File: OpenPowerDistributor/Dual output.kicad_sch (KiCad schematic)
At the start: 18 parts, among them J2 Barrel_Jack, Q1 STN2610D, Q2 BC847, Q3 BC847, U3 LM324

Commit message: More schematic progress
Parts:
- removed D7: SMBJ24A, Diode_SMD:D_SMA, symbol Diode:SMAJ12A
- added C10, C11: 100nF 16V, Capacitor_SMD:C_0603_1608Metric, symbol Device:C_Small
- added C12: NA, Capacitor_SMD:C_0603_1608Metric, symbol Device:C_Small
- added D4: SS36(F), Diode_SMD:D_SMA, symbol Device:D_Schottky
- added D6: AZ23C16, Package_TO_SOT_SMD:SOT-23, symbol Device:D_Zener_Dual_CommonAnode_KKA
- added J3: Barrel_Jack, Connector_BarrelJack:BarrelJack_Horizontal, symbol Connector:Barrel_Jack
- added Q4, Q5: BC847, Package_TO_SOT_SMD:SOT-23, symbol Transistor_BJT:BC847
- added Q6: STN2610D, Package_TO_SOT_SMD:TO-252-2, symbol Transistor_FET:IPD50R3K0CE
- added R13, R14, R15, R19: 390k, Resistor_SMD:R_0603_1608Metric, symbol Device:R_Small
- added R16, R17: 1M, Resistor_SMD:R_0603_1608Metric, symbol Device:R_Small
- added R18, R22: 100k, Resistor_SMD:R_0603_1608Metric, symbol Device:R_Small
- added R20: 15k, Resistor_SMD:R_0603_1608Metric, symbol Device:R_Small
- added R21: 33mR, Resistor_SMD:R_1206_3216Metric, symbol Device:R_Small
- C8: footprint (none) -> Capacitor_SMD:C_0603_1608Metric
- D8: footprint (none) -> Package_TO_SOT_SMD:SOT-23
- J2: footprint (none) -> Connector_BarrelJack:BarrelJack_Horizontal
- R10, R9: value 390k -> 1M; footprint (none) -> Resistor_SMD:R_0603_1608Metric
- R11: value 33k -> 100k; footprint (none) -> Resistor_SMD:R_0603_1608Metric
- R12: value 390k -> 100k; footprint (none) -> Resistor_SMD:R_0603_1608Metric
- R6, R7: footprint (none) -> Resistor_SMD:R_0603_1608Metric
- R8: value 15k -> 100k; footprint (none) -> Resistor_SMD:R_0603_1608Metric
- U3: footprint (none) -> Package_SO:TSSOP-14_4.4x5mm_P0.65mm
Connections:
- net +30V: now also R17.1
- net GND: now also Q4.2 (E), Q5.2 (E), R20.1, R21.2
- net V_{In}: now also D4.2 (A)
- net O1+: now reaches D8.2 (K), J2.1, Q1.3 (S), R11.1
- net O1+: no longer J2.2, R11.2, R5.1, U3.5 (+)
- net at R10.1, R12.2, U3.1: now also C10.2
- net at U3.10 (+): now also C11.1, R14.2
- net at U3.8: now also C11.2, R15.2, R16.1
- net Isns2: now reaches U3.9 (-)
- net Isns2: now also U3.14, C12.2, R19.1
- net O2+: now reaches U3.12 (+)
- net O2+: now also D6.2 (K), J3.1, J3.2, Q6.3 (S), R21.1, R22.1, R22.2
- net at U3.13 (-): now also C12.1, R19.2, R20.2
- net Iset: no longer names the net of U3.2 (-)
- net Iset: now also C10.1, R13.2
- net Isns renamed Isns1
- net ~{Overcurrent} renamed ~{Overcurrent}1
- new net: D6.1 (K), Q6.1 (G), R17.2, R18.1
- new net: Q5.3 (C), R18.2
- new net: D4.1 (K), Q6.2 (D)
- new net: Q5.1 (B), R16.2
- new net: Q4.1 (B), R15.1
- new net Iset1: R13.1
- new net Iset2: R14.1
- new net O1-: J2.2, R11.2, R5.1, U3.5 (+)
- new net ~{Overcurrent}2: Q4.3 (C)
- no-connect marks 1 -> 2
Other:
- note added: "Oscillation dampener"
- note added: "Output channel #1"
- note added: "Output channel #2"
- moved on the sheet: C8, C9, D4, D8, J2, Q1, Q2, Q3, R10, R11, R12, R5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

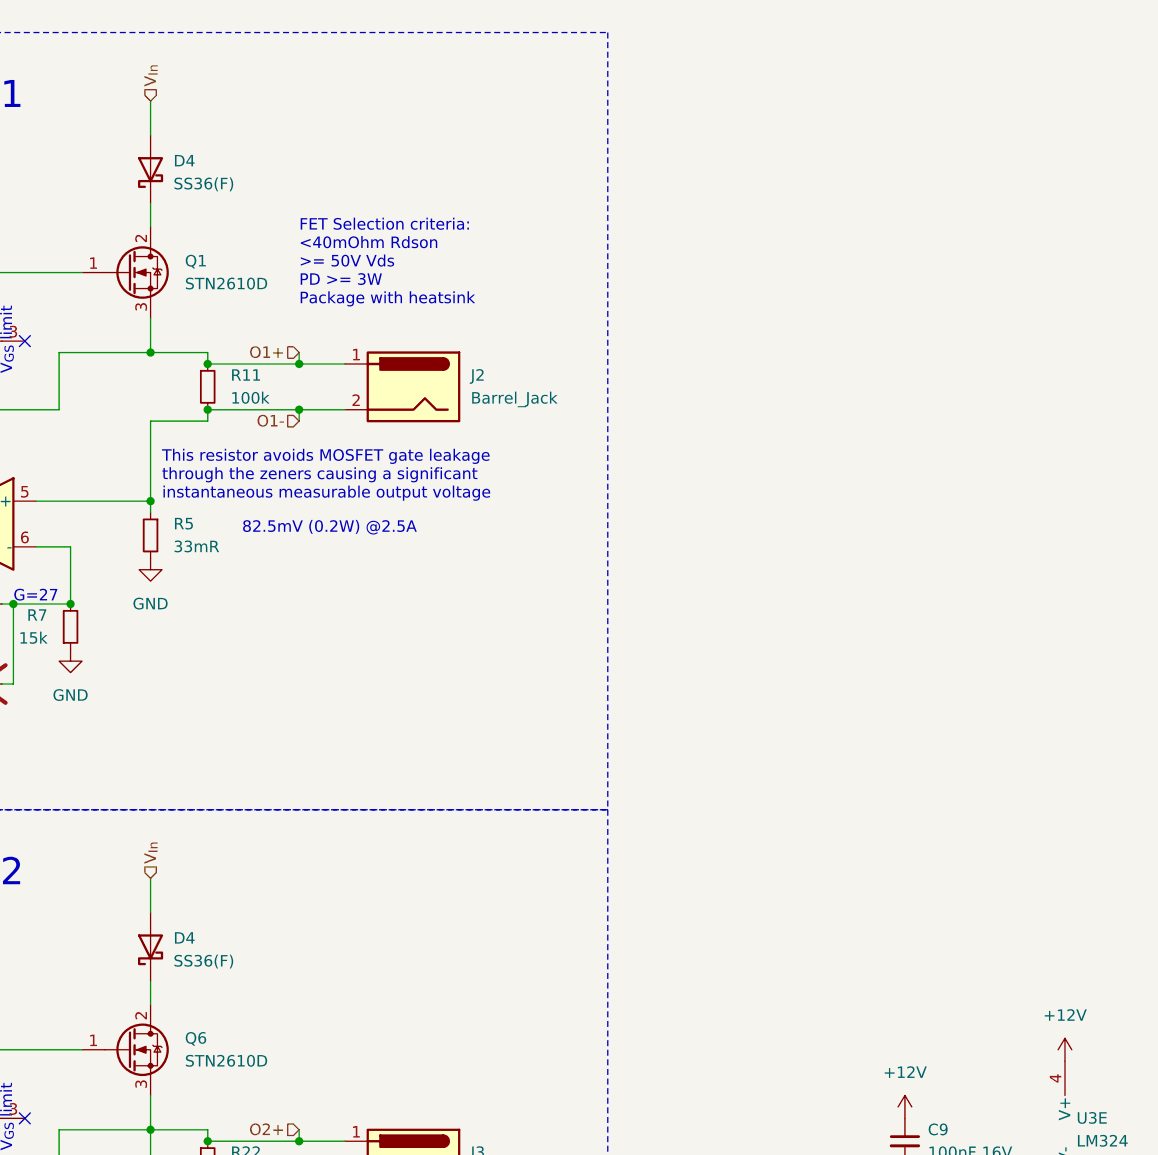
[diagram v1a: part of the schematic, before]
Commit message: Added LEDs
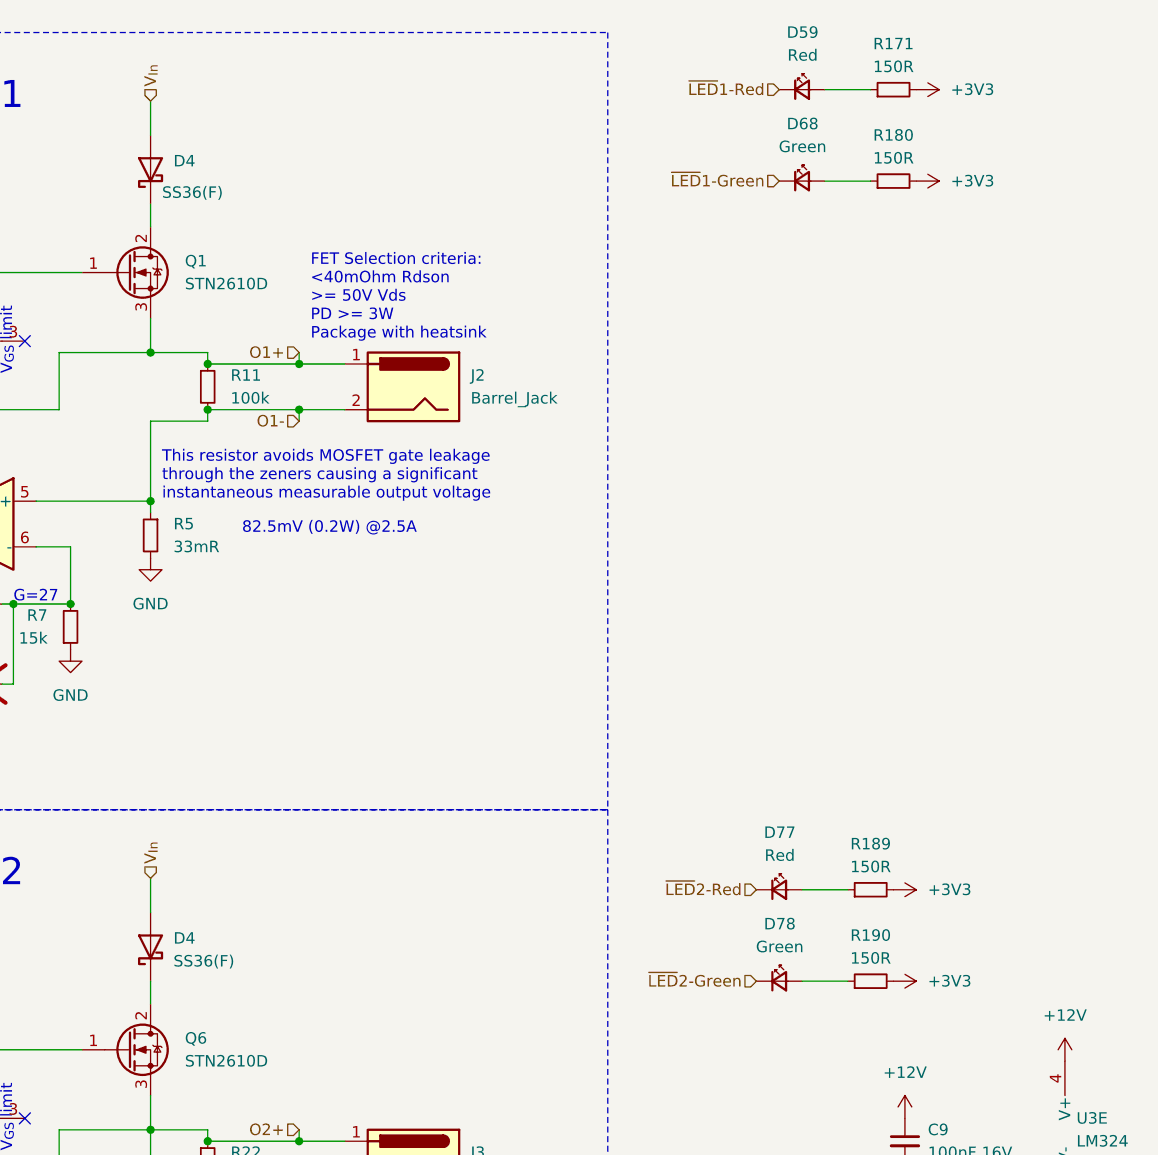
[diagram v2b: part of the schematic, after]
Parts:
- added D59, D77: Red, LED_SMD:LED_0603_1608Metric, symbol Device:LED_Small
- added D68, D78: Green, LED_SMD:LED_0603_1608Metric, symbol Device:LED_Small
- added R171, R180, R189, R190: 150R, Resistor_SMD:R_0603_1608Metric, symbol Device:R_Small
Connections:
- new net: D59.2 (A), R171.1
- new net: D68.2 (A), R180.1
- new net: D77.2 (A), R189.1
- new net: D78.2 (A), R190.1
- new net +3V3: R171.2, R180.2, R189.2, R190.2
- new net ~{LED}1-Green: D68.1 (K)
- new net ~{LED}1-Red: D59.1 (K)
- new net ~{LED}2-Green: D78.1 (K)
- new net ~{LED}2-Red: D77.1 (K)

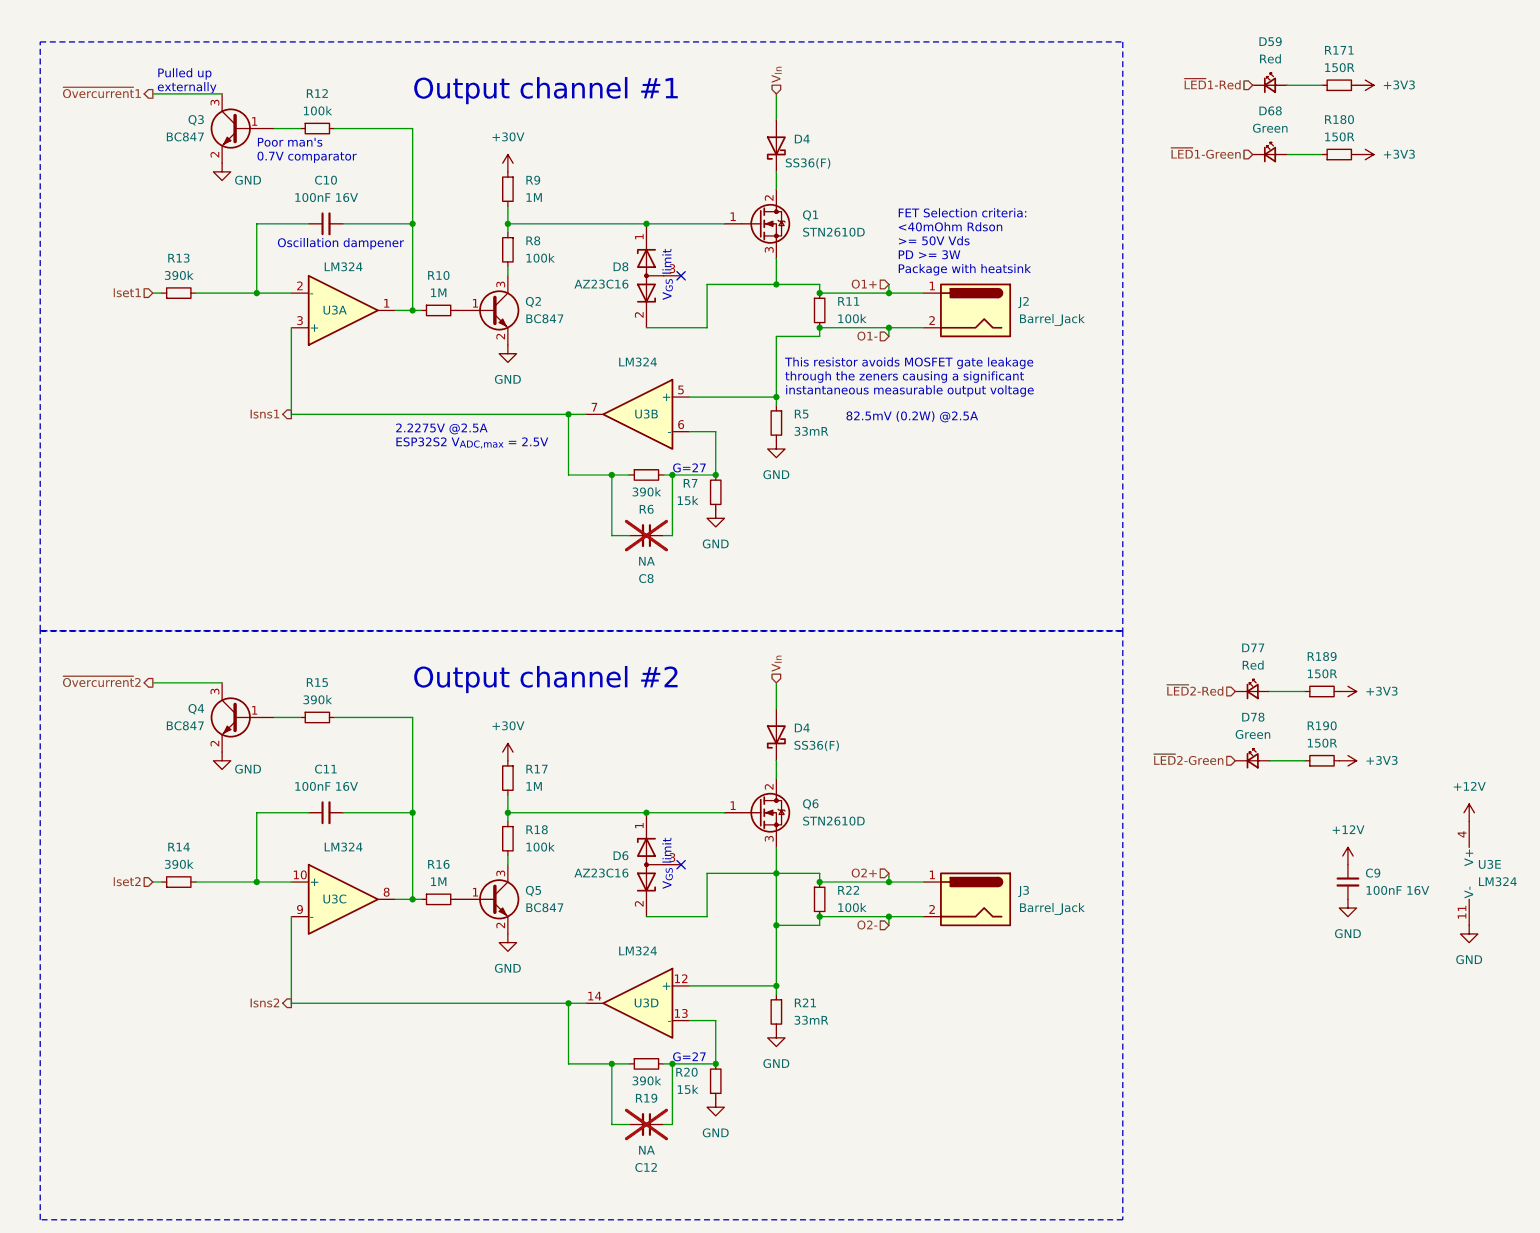
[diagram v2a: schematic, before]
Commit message: More work on schematic wiring
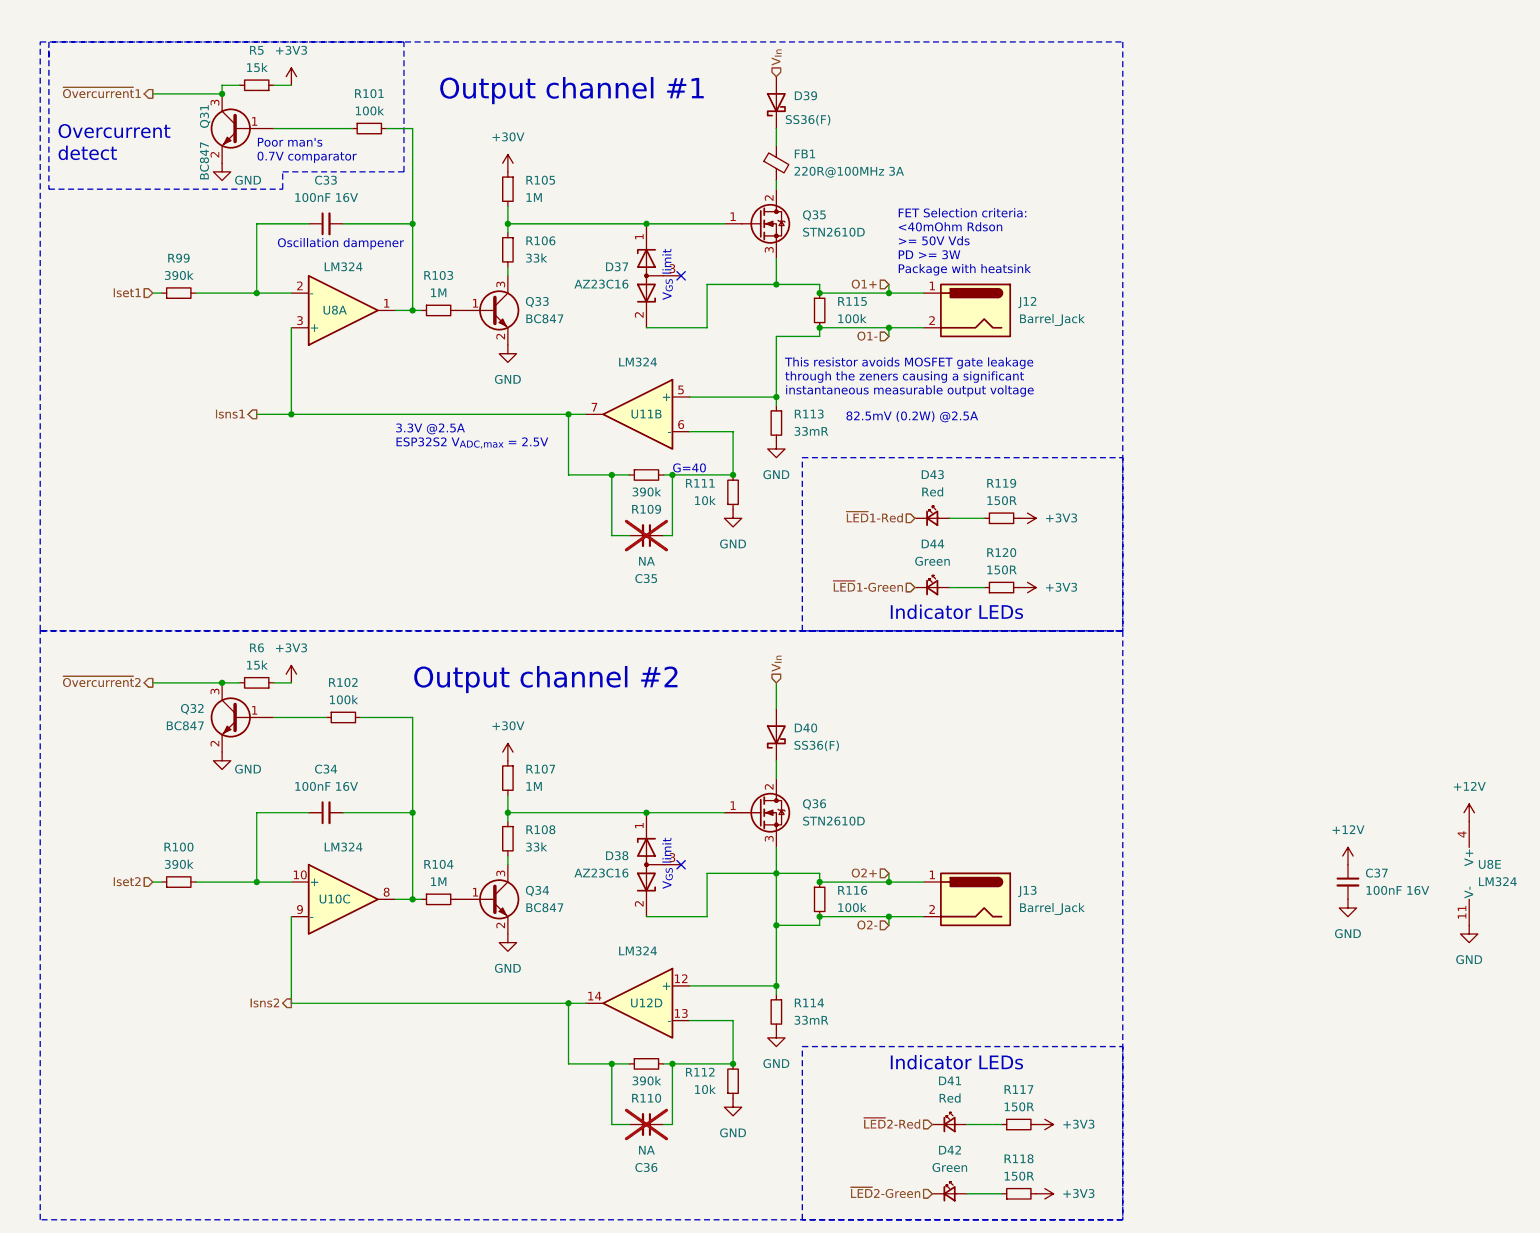
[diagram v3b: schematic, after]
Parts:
- added FB1: 220R@100MHz 3A, Inductor_SMD:L_0805_2012Metric, symbol Device:FerriteBead_Small
- added R5, R6: 15k, Resistor_SMD:R_0603_1608Metric, symbol Device:R_Small
- R102: renamed from R15; value 390k -> 100k
- R106: renamed from R8; value 100k -> 33k
- R108: renamed from R18; value 100k -> 33k
- R111: renamed from R7; value 15k -> 10k
- R112: renamed from R20; value 15k -> 10k
- renumbered C10 to C33, C11 to C34, C8 to C35, C12 to C36, C9 to C37, D8 to D37, D6 to D38, D4 to D39, D4 to D40, D77 to D41, D78 to D42, D59 to D43, D68 to D44, J2 to J12, J3 to J13, Q3 to Q31, Q4 to Q32, Q2 to Q33, Q5 to Q34, Q1 to Q35, Q6 to Q36, R14 to R100, R12 to R101, R10 to R103, R16 to R104, R9 to R105, R17 to R107, R6 to R109, R19 to R110, R5 to R113, R21 to R114, R11 to R115, R22 to R116, R189 to R117, R190 to R118, R171 to R119, R180 to R120, R13 to R99, U3 to U10, U3 to U11, U3 to U12, U3 to U8
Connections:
- net +3V3: now also R5.1, R6.1
- net ~{Overcurrent}1: now also R5.2
- net ~{Overcurrent}2: now also R6.2
- net at D39.1 (K): now also FB1.1; no longer Q35.2 (D)
- new net: FB1.2, Q35.2 (D)
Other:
- note added: "3.3V @2.5A ESP32S2 V_{ADC,max} = 2.5V"
- note added: "G=40"
- note added: "Indicator LEDs"
- note added: "Overcurrent detect"
- note removed: "2.2275V @2.5A ESP32S2 V_{ADC,max} = 2.5V"
- note removed: "G=27"
- note removed: "Pulled up externally"
- moved on the sheet: D39, D41, D42, D43, D44, R101, R102, R111, R112, R117, R118, R119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

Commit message: Start to make layout
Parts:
- added FB10: 220R@100MHz 3A, Inductor_SMD:L_0805_2012Metric, symbol Device:FerriteBead_Small
- renumbered C33 to C12, C34 to C13, C35 to C14, C36 to C15, C37 to C16, D44 to D10, D41 to D11, D42 to D12, D37 to D5, D38 to D6, D39 to D7, D40 to D8, D43 to D9, J12 to J2, J13 to J3, Q31 to Q1, Q32 to Q2, Q33 to Q3, Q34 to Q4, Q35 to Q5, Q36 to Q6, R6 to R10, R102 to R11, R101 to R12, R103 to R13, R104 to R14, R105 to R15, R106 to R16, R107 to R17, R108 to R18, R109 to R19, R110 to R20, R111 to R21, R112 to R22, R113 to R23, R114 to R24, R115 to R25, R116 to R26, R119 to R27, R120 to R28, R117 to R29, R118 to R30, R99 to R7, R100 to R8, R5 to R9, U11 to U4, U10 to U4, U8 to U4, U12 to U4
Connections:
- net at Q6.2 (D): now also FB10.2; no longer D8.1 (K)
- new net: D8.1 (K), FB10.1
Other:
- moved on the sheet: D8

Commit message: Work mostly on Ethernet schematic
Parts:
- Q5, Q6: value STN2610D -> HL20N04; footprint Package_TO_SOT_SMD:TO-252-2 -> Package_TO_SOT_SMD:SOT-89-3; LCSC Part# C2682827 -> C2688965
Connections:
- net O2+: no longer J3.2, R24.1, R26.2, U4.12 (+)
- new net O2-: J3.2, R24.1, R26.2, U4.12 (+)
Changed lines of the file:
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@@
   (junction (at 139.7 52.07) (diameter 0) (color 0 0 0 0)
   )
-  (junction (at 123.19 144.78) (diameter 0) (color 0 0 0 0)
-  )
   (junction (at 69.85 41.91) (diameter 0) (color 0 0 0 0)
   )
@@
     (stroke (width 0) (type default))
   )
-  (wire (pts (xy 123.19 137.16) (xy 123.19 144.78))
-    (stroke (width 0) (type default))
-  )
   (wire (pts (xy 54.61 128.27) (xy 46.99 128.27))
     (stroke (width 0) (type default))
@@
       (effects (font (size 1.27 1.27)) (justify left))
     )
-    (property "Value" "STN2610D" (at 127 129.54 0)
+    (property "Value" "HL20N04" (at 127 129.54 0)
       (effects (font (size 1.27 1.27)) (justify left))
     )
-    (property "Footprint" "Package_TO_SOT_SMD:TO-252-2" (at 125.73 130.175 0)
+    (property "Footprint" "Package_TO_SOT_SMD:SOT-89-3" (at 125.73 130.175 0)
       (effects (font (size 1.27 1.27) italic) (justify left) hide)
     )
@@
       (effects (font (size 1.27 1.27)) (justify left) hide)
     )
-    (property "LCSC Part#" "C2682827" (at 120.65 128.27 0)
+    (property "LCSC Part#" "C2688965" (at 120.65 128.27 0)
       (effects (font (size 1.27 1.27)) hide)
     )
@@
       (effects (font (size 1.27 1.27)) (justify left))
     )
-    (property "Value" "STN2610D" (at 127 43.18 0)
+    (property "Value" "HL20N04" (at 127 43.18 0)
       (effects (font (size 1.27 1.27)) (justify left))
     )
-    (property "Footprint" "Package_TO_SOT_SMD:TO-252-2" (at 125.73 43.815 0)
+    (property "Footprint" "Package_TO_SOT_SMD:SOT-89-3" (at 125.73 43.815 0)
       (effects (font (size 1.27 1.27) italic) (justify left) hide)
     )
@@
       (effects (font (size 1.27 1.27)) (justify left) hide)
     )
-    (property "LCSC Part#" "C2682827" (at 120.65 41.91 0)
+    (property "LCSC Part#" "C2688965" (at 120.65 41.91 0)
       (effects (font (size 1.27 1.27)) hide)
     )
